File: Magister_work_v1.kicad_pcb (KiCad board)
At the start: 4 copper layers, 50.5 x 81 mm, 151 parts, among them J1 Conn_01x02_Pin, J10 Conn_01x06_Pin, J11 Conn_01x03_Pin, J12 Conn_01x03_Pin, J13 Conn_01x03_Pin, J14 Conn_01x03_Pin, J15 Conn_01x02_Pin, J17 Conn_01x04_Pin, J2 Conn_01x03_Pin, J3 Conn_01x03_Pin, J4 Conn_01x03_Pin, J5 Conn_01x03_Pin, J6 Conn_01x04_Pin, J7 Conn_01x02_Pin, J8 Conn_01x06_Pin, J9 Conn_01x02_Pin, Q1 AO3400A, Q2 AO3400A, U10 LSM6DS3, U11 MPU-6500, U12 BMI270, U2 XC6206P332MR, U3 Ai-Thinker-Ra-01, U4 MCP6001-OT, U5 AMS1117-3.3, U6 XL1509-5.0, U7 STM32F407VETx, U8 AT24C256, U9 Ai-Thinker-Ra-01SH, Y1 X322525MQB4SI, Y2 SMD03215C2

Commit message: feat: разведены все сигнальные линии
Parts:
- moved C19 2.29 mm to (63.0, 76.2), turned to 0 degrees
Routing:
- net BN_880_RX: track 4.58 -> 46.9 mm, vias 1 -> 3
- net BN_880_TX: track 4.71 -> 45.6 mm, vias 1 -> 2
- net PWM1: track 5.17 -> 45.3 mm, vias 0 -> 1
- net PWM5: track 4.92 -> 39.6 mm, vias 0 -> 2
- net PWM7: track 5.42 -> 38.7 mm, vias 0 -> 1
- net PWM6: track 4.92 -> 36.4 mm, vias 0 -> 1
- net PWM8: track 5.36 -> 35.3 mm, vias 0 -> 1
- net PWM3: track 5.15 -> 33.9 mm, vias 0 -> 2
- net PWM2: track 5.19 -> 33.4 mm, vias 0 -> 2
- net PWM4: track 5.15 -> 22.3 mm, vias 0 -> 2
- net DIO1_RaSH: track 40.8 -> 26.3 mm
- net GND: track 128.4 -> 136.3 mm, vias 141 -> 142
- net DEBUG_TX2: track 42.9 -> 40.8 mm
- net DEBUG_RX2: track 47.2 -> 45.3 mm
- net +5V: track 37.3 -> 39.1 mm, vias 13 -> 20
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
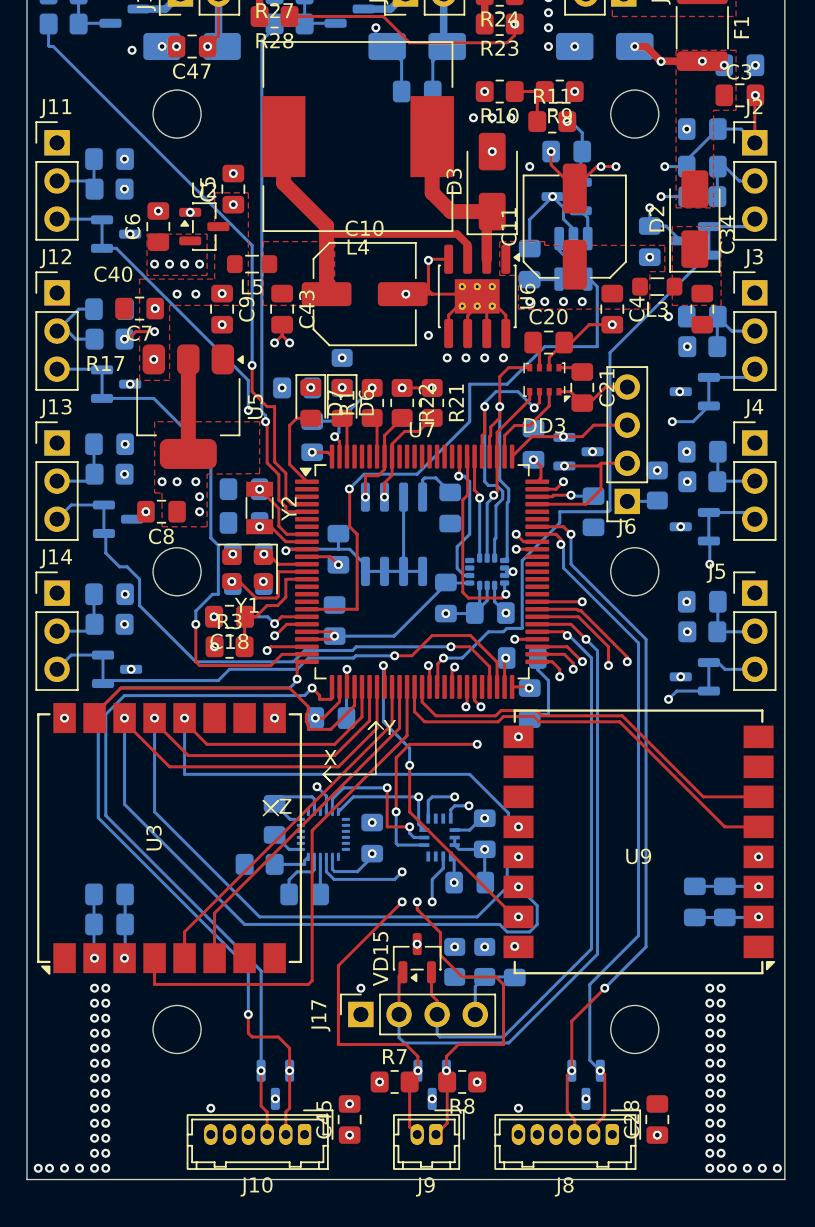
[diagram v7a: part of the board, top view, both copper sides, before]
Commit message: feat: проведены полигоны питания, 5В, 3.3А
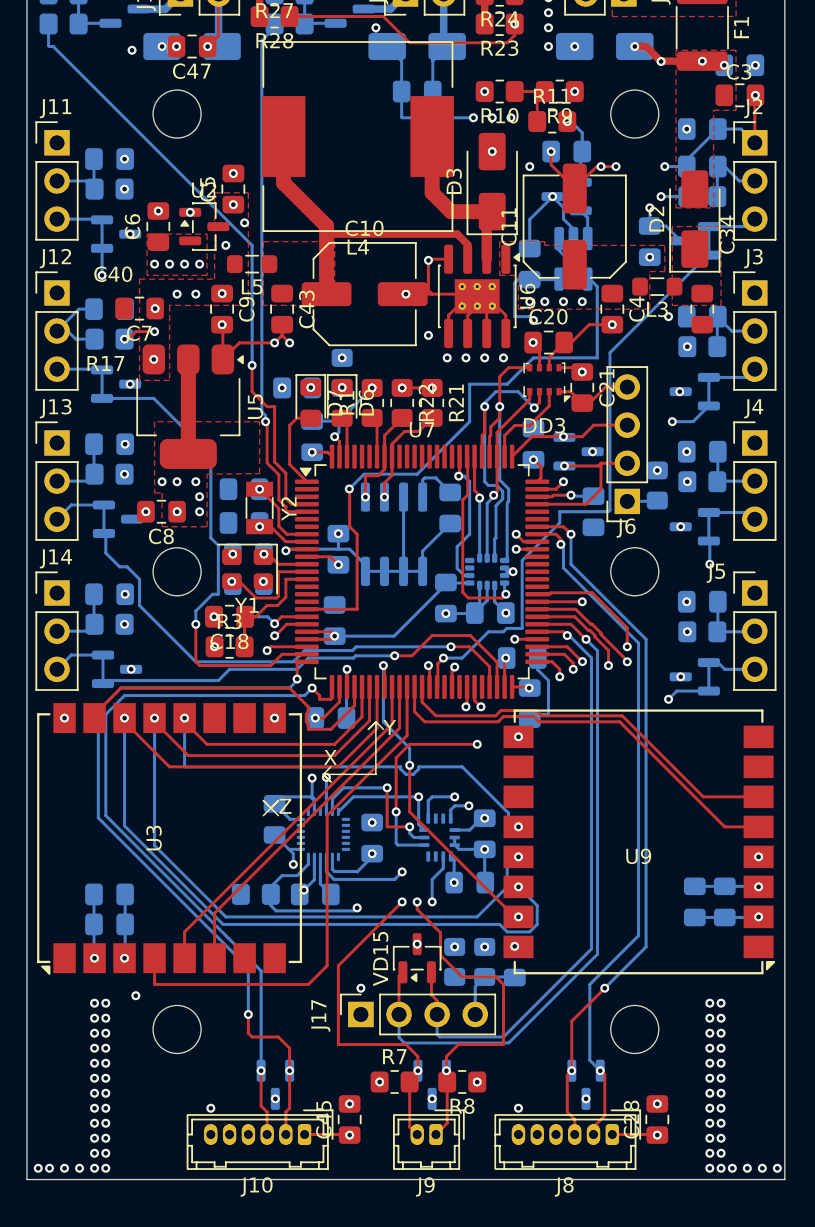
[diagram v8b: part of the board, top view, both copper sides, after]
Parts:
- moved R4 2.02 mm to (45.2, 92.0)
- moved C24 0.71 mm to (49.2, 92.0)
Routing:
- net +3V3A: track 22.1 -> 157.8 mm, vias 6 -> 9
- net +5V: track 39.1 -> 154.1 mm, vias 20 -> 23
- net MPU_INT: track 2.60 -> 54.7 mm, vias 0 -> 2
- net GND: track 136.3 -> 165.7 mm
- net PWM5: track 39.6 -> 46.0 mm
- net MISO_LoRa: track 54.7 -> 56.0 mm
- net MPU_CS: track 48.9 -> 50.0 mm
- net MOSI_LoRa: track 62.1 -> 63.0 mm
- net +3V3D: vias 25 -> 27
- added copper zone on In2.Cu, net +3V3A
- added copper zone on In2.Cu, net +5V
